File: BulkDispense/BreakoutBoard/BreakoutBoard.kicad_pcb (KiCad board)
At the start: 2 copper layers, 74.5 x 119 mm, 36 parts, among them J1 BS1, J10 OS3, J11 OS4, J12 FS1, J13 FS3, J14 PCV, J15 FS2, J16 FS4, J17 WL1, J18 WL2, J19 Analog Inputs, J2 BS2, J20 R0~R3, J21 R4~R7, J22 R8~R9, J23 Digital IN + R0~R4, J24 WB1, J25 WB2, J26 Digital Outputs, J27 R4~R9, J28 WV1, J29 WV2, J3 OS1, J30 Flow Sensors (PORT2), J4 OS2, J5 PS, J6 MV1&2, J7 MV3&4, J8 BS3, J9 BS4

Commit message: Design Overhaul
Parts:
- removed J23: Digital IN + R0~R4, PartsLibrary:CONN_37212-62M3-003PL_3MM
- removed J24: WB1, PartsLibrary:3720362A3003PL
- removed J25: WB2, PartsLibrary:3720362A3003PL
- removed J26: Digital Outputs, PartsLibrary:CONN_37212-62M3-003PL_3MM
- removed J27: R4~R9, PartsLibrary:CONN_37212-62M3-003PL_3MM
- removed J28: WV1, PartsLibrary:3720362A3003PL
- removed J29: WV2, PartsLibrary:3720362A3003PL
- removed J30: Flow Sensors (PORT2), PartsLibrary:CONN_37212-62M3-003PL_3MM
- added H5: MountingHole, MountingHole:MountingHole_3.2mm_M3, F.Cu at (181.8, 106.8)
- H1, H2, H3, H4: footprint MountingHole:MountingHole_2.2mm_M2 -> MountingHole:MountingHole_3.2mm_M3
- J1: value BS1 -> PS; footprint PartsLibrary:3720362A3003PL -> PartsLibrary:CONN_37204-62A3-004PL_3MM
- J10: value OS3 -> R0~R5; footprint PartsLibrary:3720362A3003PL -> PartsLibrary:CONN_37212-62M3-003PL_3MM
- J11: value OS4 -> WL1
- J12: value FS1 -> WL2; footprint PartsLibrary:CONN_37204-62A3-004PL_3MM -> PartsLibrary:3720362A3003PL
- J13: value FS3 -> DigitalOUT 0~3
- J14: value PCV -> DigitalOUT 4~7
- J15: value FS2 -> WB1; footprint PartsLibrary:CONN_37204-62A3-004PL_3MM -> PartsLibrary:3720362A3003PL
- J16: value FS4 -> WB2; footprint PartsLibrary:CONN_37204-62A3-004PL_3MM -> PartsLibrary:3720362A3003PL
- J17: value WL1 -> AnalogIOs; footprint PartsLibrary:3720362A3003PL -> PartsLibrary:CONN_37212-62M3-003PL_3MM
- J18: value WL2 -> WBMV1&2; footprint PartsLibrary:3720362A3003PL -> PartsLibrary:CONN_37204-62A3-004PL_3MM
- J19: value Analog Inputs -> WBMV3&4; footprint PartsLibrary:CONN_37212-62M3-003PL_3MM -> PartsLibrary:CONN_37204-62A3-004PL_3MM
- J2: value BS2 -> MV1&2; footprint PartsLibrary:3720362A3003PL -> PartsLibrary:CONN_37204-62A3-004PL_3MM
- J20: value R0~R3 -> FS1
- J21: value R4~R7 -> FS2~FS4; footprint PartsLibrary:CONN_37204-62A3-004PL_3MM -> PartsLibrary:CONN_37212-62M3-003PL_3MM
- J22: value R8~R9 -> WB-MV5&6; footprint PartsLibrary:CONN_37204-62A3-004PL_3MM -> PartsLibrary:3720362A3003PL
- J3: value OS1 -> MV3&4; footprint PartsLibrary:3720362A3003PL -> PartsLibrary:CONN_37204-62A3-004PL_3MM
- J4: value OS2 -> RV1~4; footprint PartsLibrary:3720362A3003PL -> PartsLibrary:CONN_37204-62A3-004PL_3MM
- J5: value PS -> PCV
- J6: value MV1&2 -> FS1
- J7: value MV3&4 -> FS3
- J8: value BS3 -> FS2; footprint PartsLibrary:3720362A3003PL -> PartsLibrary:CONN_37204-62A3-004PL_3MM
- J9: value BS4 -> FS4; footprint PartsLibrary:3720362A3003PL -> PartsLibrary:CONN_37204-62A3-004PL_3MM
- moved H3 138.4 mm to (181.6, 32.0)
- moved J12 86.9 mm to (170.4, 47.8)
- moved H4 84.8 mm to (106.8, 106.8)
- moved J15 80.6 mm to (154.6, 38.6)
- moved J16 80.4 mm to (154.6, 47.8)
- moved J5 78.6 mm to (148.7, 57.8)
- moved J6 78.5 mm to (153.4, 74.4), turned to 90 degrees
- moved J7 76.5 mm to (167.8, 74.4), turned to 90 degrees
- moved H2 73.1 mm to (106.8, 31.8)
- moved D1 71.6 mm to (136.0, 99.6)
- moved R1 71.6 mm to (136.5, 102.1)
- moved J3 62.7 mm to (160.4, 94.4), turned to 90 degrees
- moved J14 62.7 mm to (122.5, 73.0), turned to -90 degrees
- moved J13 54.5 mm to (129.6, 73.0), turned to -90 degrees
- moved H1 49.3 mm to (144.2, 69.0)
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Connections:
- J1 pad 3: /AI0 -> GND
- J10 pad 2: GND -> +24V
- J10 pad 3: /DI2 -> +24V
- J11 pad 3: /DI3 -> /AI6
- J12 pad 1: /FS1-1 -> +24V
- J12 pad 2: /FS1-2 -> GND
- J12 pad 3: /FS1-3 -> /AI7
- J13 pad 1: /FS3-1 -> /DO0
- J13 pad 2: /FS3-2 -> /DO1
- J13 pad 3: /FS3-3 -> /DO2
- J13 pad 4: /FS3-4 -> /DO3
- J14 pad 1: +24V -> /DO4
- J14 pad 2: /AI13 -> /DO5
- J14 pad 3: /AO0 -> /DO6
- J14 pad 4: GND -> /DO7
- J15 pad 1: /FS2-1 -> +24V
- J15 pad 2: /FS2-2 -> GND
- J15 pad 3: /FS2-3 -> /AI4
- J16 pad 1: /FS4-1 -> +24V
- J16 pad 2: /FS4-2 -> GND
- J16 pad 3: /FS4-3 -> /AI5
- J17 pad 1: +24V -> /AI4
- J17 pad 2: GND -> /AI5
- J18 pad 1: +24V -> /DO4
- J18 pad 3: /AI7 -> /DO5
- J19 pad 1: /AI0 -> /DO6
- J19 pad 2: /AI1 -> GND
- J19 pad 3: /AI2 -> /DO7
- J19 pad 4: /AI3 -> GND
- J19 pad 5: /AI4 -> (no net)
- J19 pad 6: /AI5 -> (no net)
- J2 pad 1: +24V -> /DO0
- J2 pad 3: /AI1 -> /DO1
- J20 pad 1: /R0_OUT -> /FS1-1
- J20 pad 2: /R1_OUT -> /FS1-2
- J20 pad 3: /R2_OUT -> /FS1-3
- J20 pad 4: /R3_OUT -> /FS1-4
- J21 pad 1: /R4_OUT -> /FS2-1
- J21 pad 2: /R5_OUT -> /FS2-2
- J21 pad 3: /R6_OUT -> /FS2-3
- J21 pad 4: /R7_OUT -> /FS2-4
- J21 pad 5: (no net) -> /FS3-1
- J21 pad 6: (no net) -> /FS3-2
- J22 pad 1: /R8_OUT -> /R4_OUT
- J22 pad 2: /R9_OUT -> unconnected-(J22-Pin_2-Pad2)
- J22 pad 3: GND -> /R5_OUT
- J3 pad 1: +24V -> /DO2
- J3 pad 3: /DI0 -> /DO3
- J4 pad 1: +24V -> /R0_OUT
- J4 pad 2: GND -> /R1_OUT
- J4 pad 3: /DI1 -> /R2_OUT
- J5 pad 2: GND -> /AI13
- J5 pad 3: GND -> /AO0
- J5 pad 4: /AI12 -> GND
- J6 pad 1: /DO0 -> /FS1-1
- J6 pad 2: GND -> /FS1-2
- J6 pad 3: /DO1 -> /FS1-3
- J6 pad 4: GND -> /FS1-4
- J7 pad 1: /DO2 -> /FS3-1
- J7 pad 2: GND -> /FS3-2
- J7 pad 3: /DO3 -> /FS3-3
- J7 pad 4: GND -> /FS3-4
- J8 pad 1: +24V -> /FS2-1
- J8 pad 2: GND -> /FS2-2
- J8 pad 3: /AI2 -> /FS2-3
- J9 pad 1: +24V -> /FS4-1
- J9 pad 2: GND -> /FS4-2
- J9 pad 3: /AI3 -> /FS4-3
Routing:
- net +24V: track 306.2 -> 151.7 mm, vias 3 -> 0
- net /DO1: track 121.7 -> 35.4 mm, vias 0 -> 1
- net /DO0: track 126.8 -> 41.1 mm, vias 0 -> 1
- net /R6_OUT: track 69.9 -> 0.00 mm
- net /DO6: track 0.00 -> 65.3 mm
- net /DO4: track 0.00 -> 64.6 mm, vias 0 -> 1
- net /R7_OUT: track 61.6 -> 0.00 mm
- net /AI6: track 54.5 -> 115.9 mm
- net /AI0: track 60.2 -> 0.00 mm, vias 1 -> 0
- net /R5_OUT: track 69.4 -> 9.38 mm
- net /AI8: track 59.9 -> 0.00 mm, vias 1 -> 0
- net /DO5: track 0.00 -> 58.0 mm
- net /DO7: track 0.00 -> 57.0 mm
- net /R4_OUT: track 69.0 -> 12.5 mm
- net /DO3: track 91.4 -> 35.8 mm, vias 0 -> 1
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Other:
- board size 74.5 x 119 mm -> 80 x 80 mm
- board text added: "ANALOG"
- board text added: "DIGITAL"
- board text added: "FS1"
- board text added: "FS2~4"
- board text added: "IN"
- board text added: "ON"
- board text added: "OUT"
- board text added: "R0~R5"
- board text added: "WB1"
- board text added: "WB2"
- board text added: "WBMV5&6"
- board text added: "WL1"
- board text added: "WL2"
- board text removed: "Analog IN (PORT4)"
- board text removed: "Digital IN"
- board text removed: "Digital OUT (PORT1)"
- board text removed: "Power"
- board text removed: "R0~R4 (PORT3)"
- board text removed: "R4~R9 (PORT5)"

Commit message: Add latest design
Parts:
- added J24: LDS, PartsLibrary:CONN_37204-62A3-004PL_3MM, F.Cu at (146.2, 74.4)
- J11, J12, J15, J16, J22: footprint PartsLibrary:3720362A3003PL -> PartsLibrary:CONN_37203-62A3-003PL_3MM
- J18: value WBMV1&2 -> WB-MV1&2
- J19: value WBMV3&4 -> WB-MV3&4
- moved H1 5.42 mm to (138.8, 69.0)
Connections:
- J17 pad 10: +24V -> /LDS
- J17 pad 11: unconnected-(J17-Pin_11-Pad11) -> +24V
- J17 pad 7: unconnected-(J17-Pin_7-Pad7) -> /AO0
- J17 pad 8: /AO0 -> /LDS-5V
- J17 pad 9: unconnected-(J17-Pin_9-Pad9) -> /LDS-GND
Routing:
- net GND: track 1.23 -> 37.6 mm
- net /LDS-GND: track 0.00 -> 35.5 mm, vias 0 -> 1
- net /LDS-5V: track 0.00 -> 29.7 mm, vias 0 -> 1
- net /LDS: track 0.00 -> 25.1 mm, vias 0 -> 1
- net /FS1-2: track 40.3 -> 53.6 mm, vias 0 -> 2
- net /FS4-1: track 55.1 -> 64.1 mm, vias 0 -> 1
- net /AI5: track 72.4 -> 80.1 mm
- net +24V: track 151.7 -> 159.2 mm
- net /R0_OUT: track 59.6 -> 52.4 mm, vias 1 -> 2
- net /FS1-3: track 45.7 -> 52.7 mm, vias 0 -> 1
- net /AI4: track 91.5 -> 97.8 mm, vias 1 -> 2
- net /FS4-4: track 50.7 -> 44.8 mm, vias 0 -> 1
- net /DO2: track 42.3 -> 48.2 mm
- net /DO6: track 65.3 -> 71.1 mm, vias 0 -> 1
- net /AI7: track 85.4 -> 90.9 mm, vias 2 -> 1
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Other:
- board text added: "LDS"
- board text added: "WB MV1&2"
- board text added: "WB MV3&4"
- board text added: "WB MV5&6"
- board text removed: "WBMV5&6"

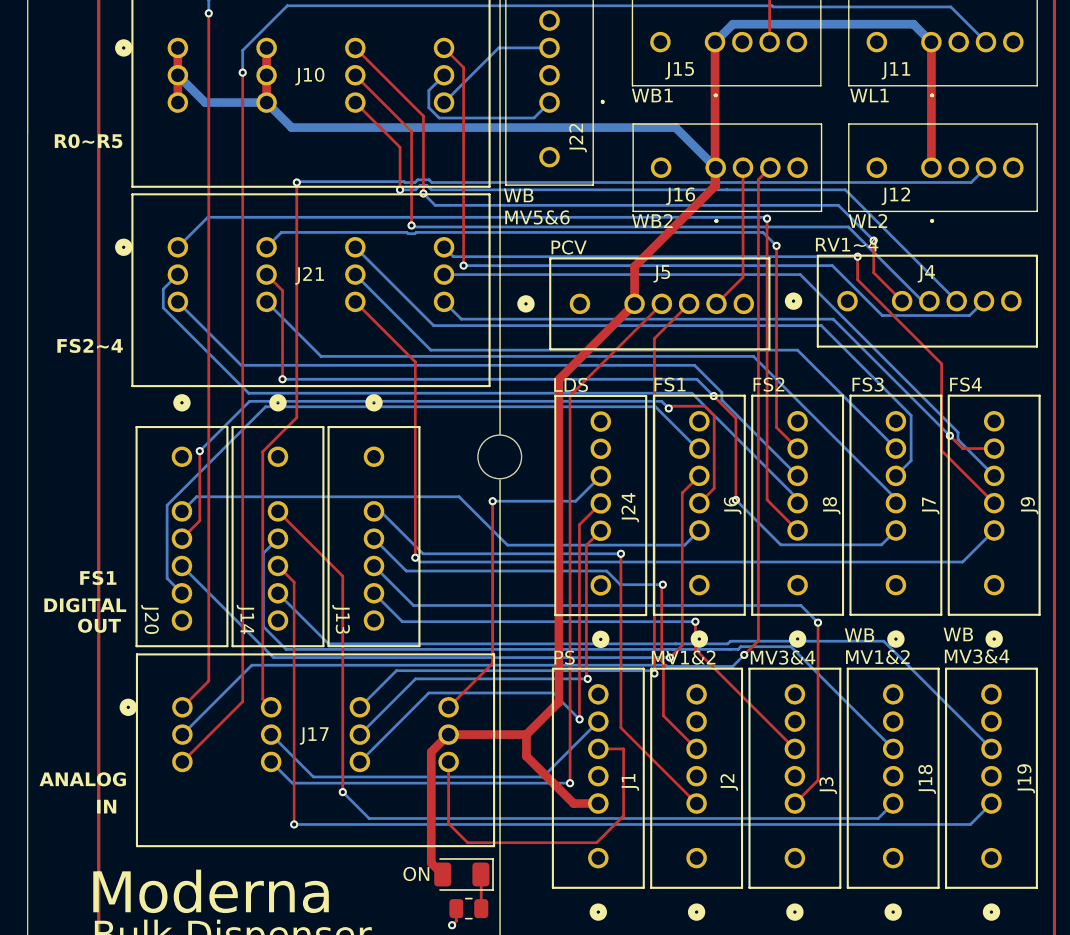
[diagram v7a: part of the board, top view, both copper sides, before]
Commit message: Update PCB + Add Lynx Wiring Diagram
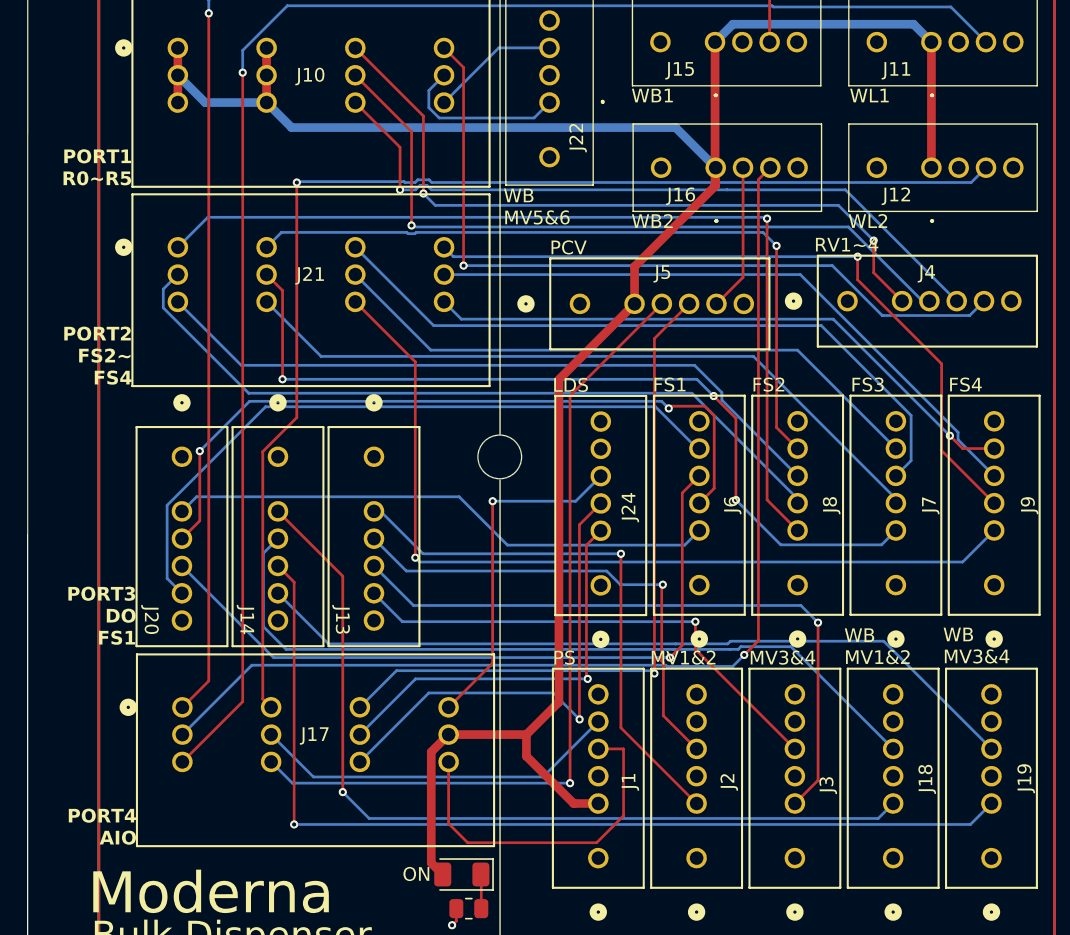
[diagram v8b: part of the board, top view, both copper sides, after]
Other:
- board text added: "PORT1 R0~R5"
- board text added: "PORT2 FS2~ FS4"
- board text added: "PORT3 DO FS1"
- board text added: "PORT4 AIO"
- board text removed: "ANALOG"
- board text removed: "DIGITAL"
- board text removed: "FS1"
- board text removed: "FS2~4"
- board text removed: "IN"
- board text removed: "OUT"
- board text removed: "R0~R5"
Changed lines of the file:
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@@
 				(font
 					(size 1 1)
-					(thickness 0.15)
+					(thickness 0.125)
 				)
 			)
@@
 				(font
 					(size 1 1)
-					(thickness 0.15)
+					(thickness 0.125)
 				)
 			)
@@
 				(font
 					(size 1 1)
-					(thickness 0.15)
+					(thickness 0.125)
 				)
 			)
@@
 				(font
 					(size 1 1)
-					(thickness 0.15)
+					(thickness 0.125)
 				)
 			)
@@
 				(font
 					(size 1 1)
-					(thickness 0.15)
+					(thickness 0.125)
 				)
 			)
@@
 				(font
 					(size 1 1)
-					(thickness 0.15)
+					(thickness 0.125)
 				)
 			)
@@
 				(font
 					(size 1 1)
-					(thickness 0.15)
+					(thickness 0.125)
 				)
 			)
@@
 				(font
 					(size 1 1)
-					(thickness 0.15)
+					(thickness 0.125)
 				)
 			)
@@
 				(font
 					(size 1 1)
-					(thickness 0.15)
+					(thickness 0.125)
 				)
 			)
@@
 		(layer "Edge.Cuts")
 	)
-	(gr_text "IN"
-		(at 109.154763 95.25 0)
-		(layer "F.SilkS")
-		(effects
-			(font
-				(size 1 1)
-				(thickness 0.2)
-				(bold yes)
-			)
-			(justify left bottom)
-		)
-	)
 	(gr_text "WB2"
 		(at 150 51.775 0)
@@
 			(font
 				(size 1 1)
-				(thickness 0.15)
+				(thickness 0.125)
 			)
 		)
@@
 		)
 	)
-	(gr_text "WL1"
-		(at 165.9 42.575 0)
+	(gr_text "PORT4\nAIO"
+		(at 112.202398 97.523099 0)
 		(layer "F.SilkS")
 		(effects
 			(font
 				(size 1 1)
-				(thickness 0.15)
+				(thickness 0.2)
+				(bold yes)
 			)
+			(justify right bottom)
 		)
 	)
-	(gr_text "OUT"
-		(at 107.821429 82 0)
+	(gr_text "WL1"
+		(at 165.9 42.575 0)
 		(layer "F.SilkS")
 		(effects
 			(font
 				(size 1 1)
-				(thickness 0.2)
-				(bold yes)
+				(thickness 0.125)
 			)
-			(justify left bottom)
 		)
 	)
@@
 		)
 	)
-	(gr_text "FS1"
-		(at 107.916667 78.5 0)
+	(gr_text "PORT3\nDO\nFS1"
+		(at 112.1726 82.8764 0)
 		(layer "F.SilkS")
 		(effects
@@
 				(bold yes)
 			)
-			(justify left bottom)
+			(justify right bottom)
 		)
 	)
@@
 			(font
 				(size 1 1)
-				(thickness 0.15)
+				(thickness 0.125)
 			)
 			(justify left bottom)
@@
 		)
 	)
-	(gr_text "ANALOG"
-		(at 105.059524 93.25 0)
-		(layer "F.SilkS")
-		(effects
-			(font
-				(size 1 1)
-				(thickness 0.2)
-				(bold yes)
-			)
-			(justify left bottom)
-		)
-	)
-	(gr_text "DIGITAL"
-		(at 105.29762 80.5 0)
-		(layer "F.SilkS")
-		(effects
-			(font
-				(size 1 1)
-				(thickness 0.2)
-				(bold yes)
-			)
-			(justify left bottom)
-		)
-	)
 	(gr_text "Moderna"
 		(at 108.6 102.735 0)
@@
 			(font
 				(size 1 1)
-				(thickness 0.15)
+				(thickness 0.125)
 			)
 		)
@@
 			(font
 				(size 1 1)
-				(thickness 0.15)
+				(thickness 0.125)
 			)
 			(justify left)
@@
 		)
 	)
-	(gr_text "R0~R5"
-		(at 106.059524 46.5 0)
+	(gr_text "PORT1\nR0~R5"
+		(at 111.868998 49.223099 0)
 		(layer "F.SilkS")
 		(effects
@@
 				(bold yes)
 			)
-			(justify left bottom)
+			(justify right bottom)
 		)
 	)
-	(gr_text "FS2~4"
-		(at 106.25 61.5 0)
+	(gr_text "PORT2\nFS2~\nFS4"
+		(at 111.868998 63.823099 0)
 		(layer "F.SilkS")
 		(effects
@@
 				(bold yes)
 			)
-			(justify left bottom)
+			(justify right bottom)
 		)
 	)
